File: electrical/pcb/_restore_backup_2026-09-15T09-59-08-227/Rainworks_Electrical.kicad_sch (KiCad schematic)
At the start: 19 parts, among them J1 472192001, P1 ESP8266 Thing, U1 MCP3008, U10 S1_SM, U11 S0_PH, U7 S4_FR, U8 S3_T, U9 S2_C

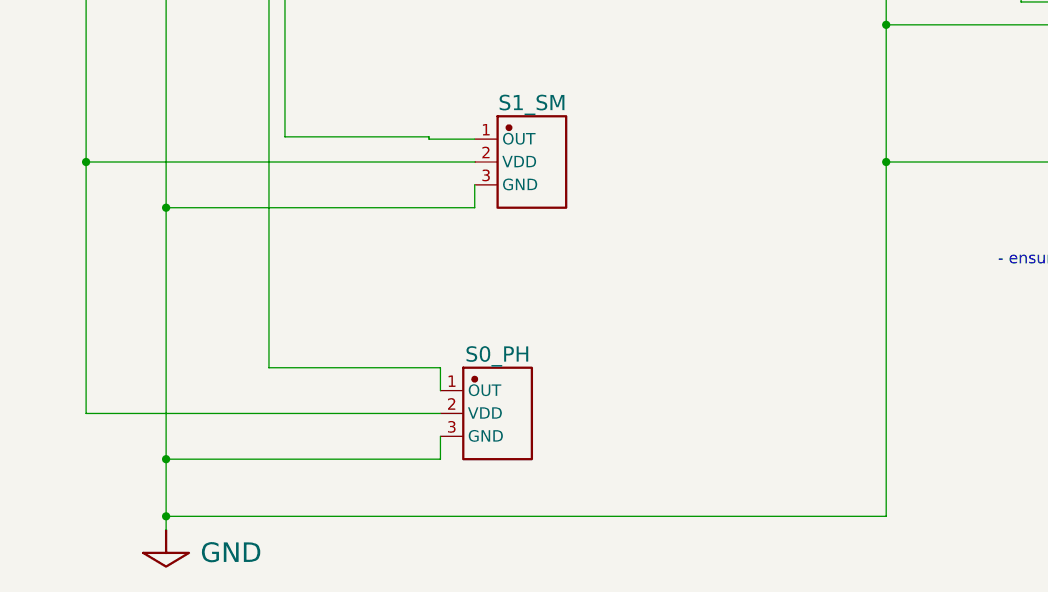
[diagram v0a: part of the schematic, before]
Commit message: Adding SD card passives and preparing for autorouter outside of KiCad, includes placement and schematic ERC checks
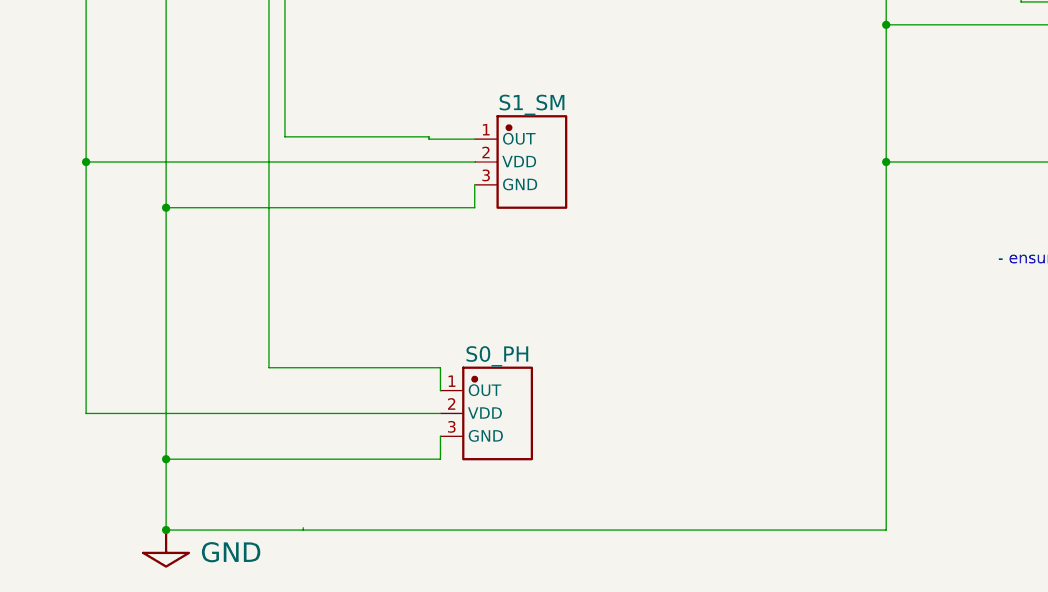
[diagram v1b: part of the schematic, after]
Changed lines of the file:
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@@
+	)
+	(junction
+		(at 135.89 146.05)
+		(diameter 0)
+		(color 0 0 0 0)
 	)
 	(junction
@@
 	)
 	(junction
-		(at 135.89 146.05)
-		(diameter 0)
-		(color 0 0 0 0)
-	)
-	(junction
 		(at 165.1 146.05)
 		(diameter 0)
@@
 	)
 	(junction
-		(at 55.88 185.42)
+		(at 55.88 186.944)
 		(diameter 0)
 		(color 0 0 0 0)
@@
 	(wire
 		(pts
-			(xy 55.88 186.944) (xy 55.88 185.42)
+			(xy 55.88 186.944) (xy 55.88 179.07)
 		)
 		(stroke
@@
 	(wire
 		(pts
-			(xy 55.88 185.42) (xy 55.88 179.07)
-		)
-		(stroke
-			(width 0)
-			(type default)
-		)
-	)
-	(wire
-		(pts
 			(xy 88.9 118.11) (xy 88.9 115.57)
 		)
@@
 	(wire
 		(pts
+			(xy 55.88 186.944) (xy 135.89 186.944)
+		)
+		(stroke
+			(width 0)
+			(type default)
+		)
+	)
+	(wire
+		(pts
 			(xy 127 125.73) (xy 165.1 125.73)
 		)
@@
 	(wire
 		(pts
-			(xy 55.88 185.42) (xy 135.89 185.42)
-		)
-		(stroke
-			(width 0)
-			(type default)
-		)
-	)
-	(wire
-		(pts
 			(xy 213.36 133.604) (xy 213.36 133.35)
 		)
@@
 	(wire
 		(pts
+			(xy 71.12 186.69) (xy 71.12 186.944)
+		)
+		(stroke
+			(width 0)
+			(type default)
+		)
+	)
+	(wire
+		(pts
 			(xy 255.524 56.896) (xy 255.524 57.15)
 		)
@@
 	(wire
 		(pts
-			(xy 135.89 146.05) (xy 135.89 185.42)
-		)
-		(stroke
+			(xy 135.89 146.05) (xy 135.89 186.944)
+		)
+		(stroke
